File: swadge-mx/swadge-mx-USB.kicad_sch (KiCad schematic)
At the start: 6 parts, among them P1 USB_C_Plug_USB2.0

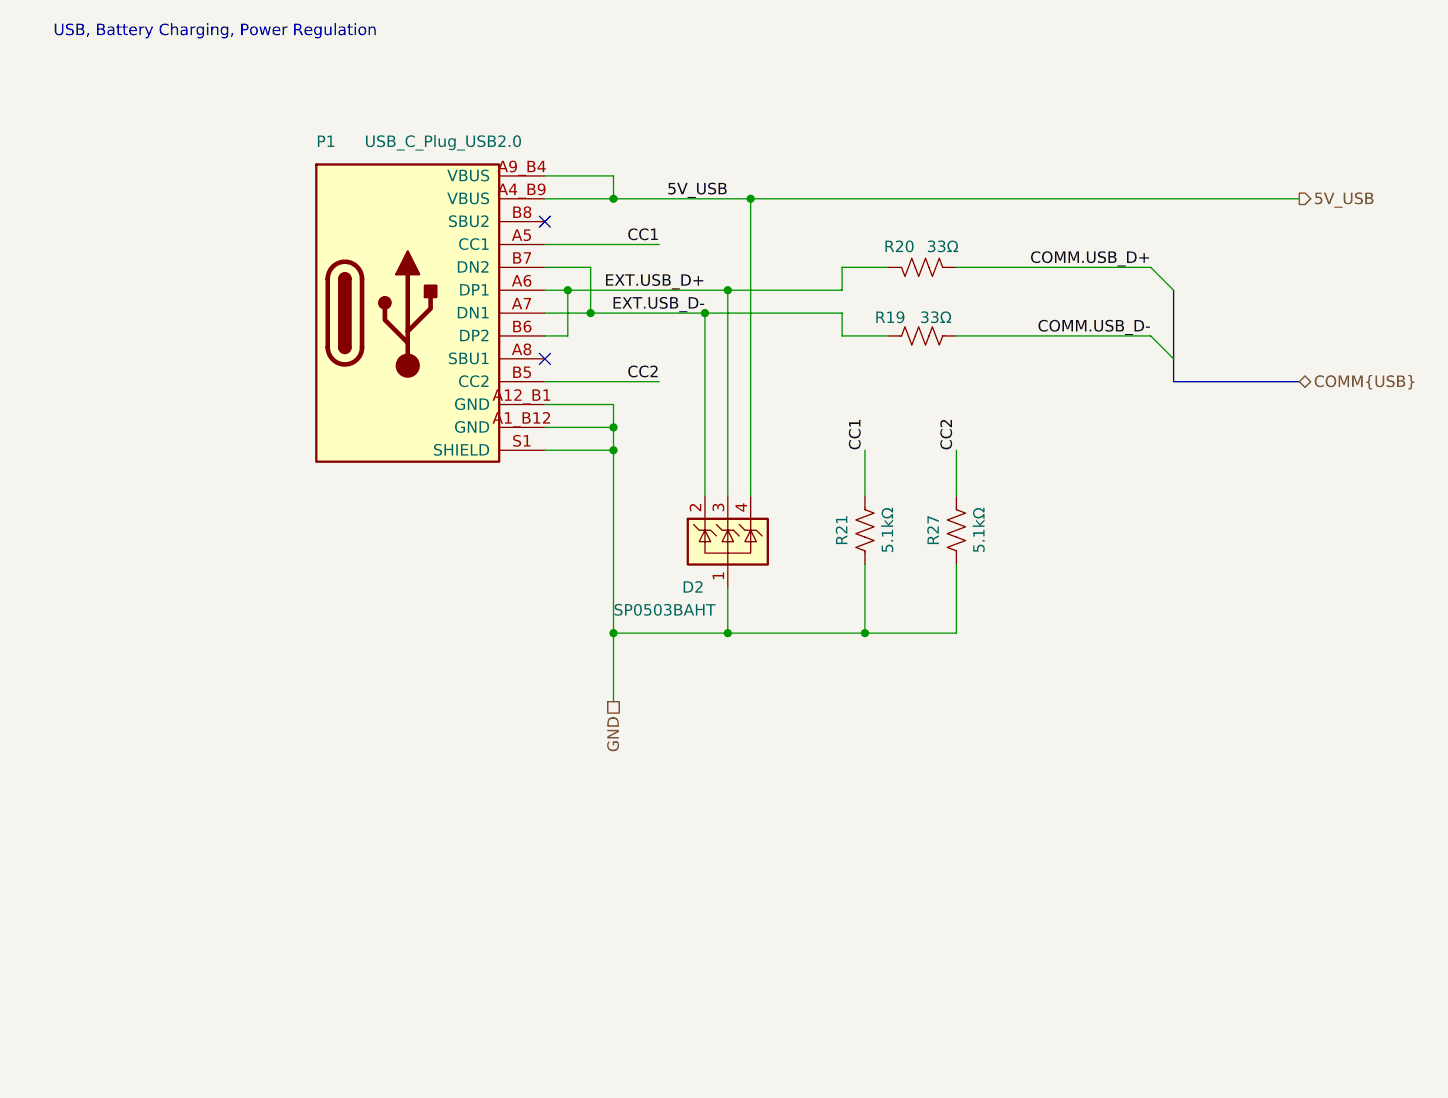
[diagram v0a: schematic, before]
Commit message: Further Subdivide Sheets
Moved all audio into one sheet, and sub-divided into DAC and amp sheets. Moved all power into one sheet and sub-divided into BMS and Buck.
Cleaned up front page a bit.
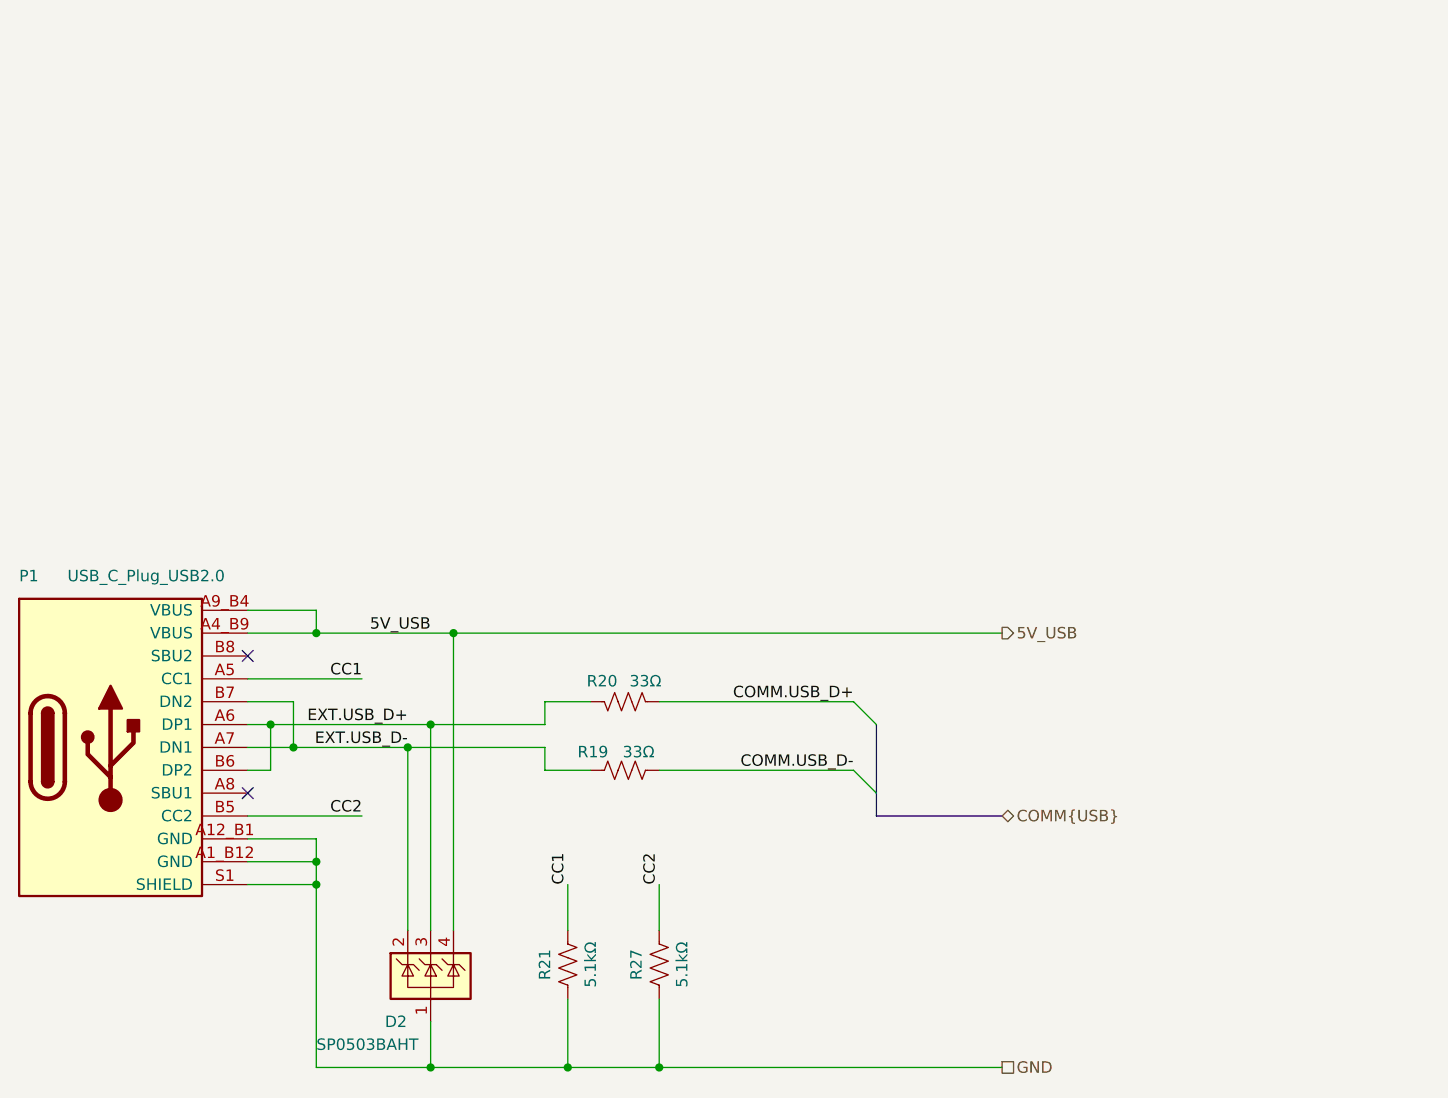
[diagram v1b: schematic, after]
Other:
- note removed: "USB, Battery Charging, Power Regulation"
- moved on the sheet: D2, P1, R19, R20, R21, R27
